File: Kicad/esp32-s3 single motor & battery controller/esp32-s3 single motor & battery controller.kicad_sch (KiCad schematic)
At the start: 61 parts, among them J1 JST SH SM04B/Qwiic, J2 7 pin FPC 0.3mm, J3 Conn_01x03, J4 Conn_01x03, SW1 KMR2, SW2 KMR2, U5 ESP32-S3, U6 74HC595, Y1 40mhz, 10ppm

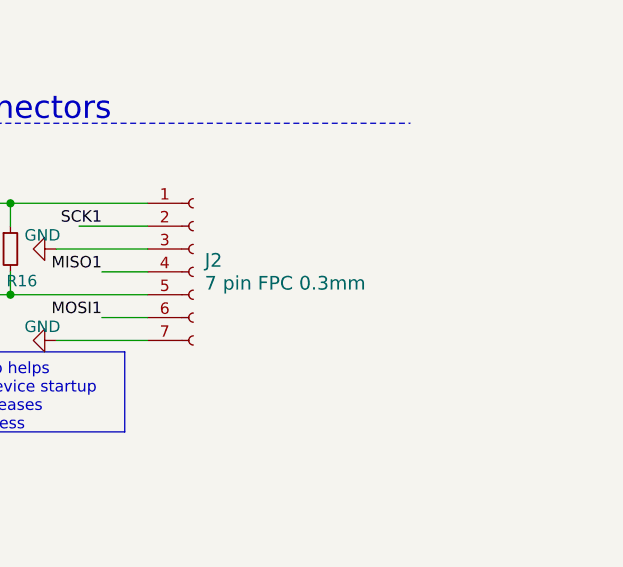
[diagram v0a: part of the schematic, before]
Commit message: Updated README with current progress and V2 pcb
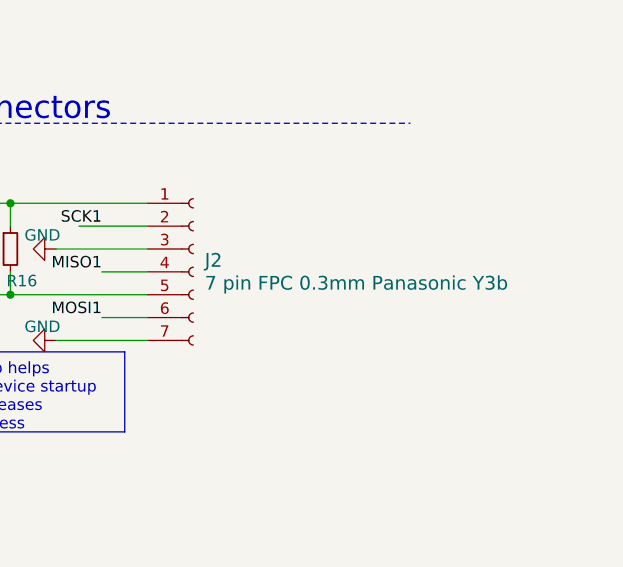
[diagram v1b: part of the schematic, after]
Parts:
- J2: value 7 pin FPC 0.3mm -> 7 pin FPC 0.3mm Panasonic Y3b
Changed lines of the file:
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@@
 			)
 		)
-		(property "Value" "7 pin FPC 0.3mm"
+		(property "Value" "7 pin FPC 0.3mm Panasonic Y3b"
 			(at 261.62 91.4399 0)
 			(effects

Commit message: Gerbers and BOM for v0.4 PCB
I adjusted all the testpoints to be excluded from the BOM.
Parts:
- TP1, TP10, TP11, TP12, TP14, TP15, TP19, TP20, TP21, TP24, TP25, TP26, TP27, TP28, TP29, TP30, TP5, TP7, TP8, TP9: now left out of the parts list
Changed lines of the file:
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@@
 		(unit 1)
 		(exclude_from_sim no)
-		(in_bom yes)
+		(in_bom no)
 		(on_board yes)
 		(dnp no)
@@
 		(unit 1)
 		(exclude_from_sim no)
-		(in_bom yes)
+		(in_bom no)
 		(on_board yes)
 		(dnp no)
@@
 		(unit 1)
 		(exclude_from_sim no)
-		(in_bom yes)
+		(in_bom no)
 		(on_board yes)
 		(dnp no)
@@
 		(unit 1)
 		(exclude_from_sim no)
-		(in_bom yes)
+		(in_bom no)
 		(on_board yes)
 		(dnp no)
@@
 		(unit 1)
 		(exclude_from_sim no)
-		(in_bom yes)
+		(in_bom no)
 		(on_board yes)
 		(dnp no)
@@
 		(unit 1)
 		(exclude_from_sim no)
-		(in_bom yes)
+		(in_bom no)
 		(on_board yes)
 		(dnp no)
@@
 		(unit 1)
 		(exclude_from_sim no)
-		(in_bom yes)
+		(in_bom no)
 		(on_board yes)
 		(dnp no)
@@
 		(unit 1)
 		(exclude_from_sim no)
-		(in_bom yes)
+		(in_bom no)
 		(on_board yes)
 		(dnp no)
@@
 		(unit 1)
 		(exclude_from_sim no)
-		(in_bom yes)
+		(in_bom no)
 		(on_board yes)
 		(dnp no)
@@
 		(unit 1)
 		(exclude_from_sim no)
-		(in_bom yes)
+		(in_bom no)
 		(on_board yes)
 		(dnp no)
@@
 		(unit 1)
 		(exclude_from_sim no)
-		(in_bom yes)
+		(in_bom no)
 		(on_board yes)
 		(dnp no)
@@
 		(unit 1)
 		(exclude_from_sim no)
-		(in_bom yes)
+		(in_bom no)
 		(on_board yes)
 		(dnp no)
@@
 		(unit 1)
 		(exclude_from_sim no)
-		(in_bom yes)
+		(in_bom no)
 		(on_board yes)
 		(dnp no)
@@
 		(unit 1)
 		(exclude_from_sim no)
-		(in_bom yes)
+		(in_bom no)
 		(on_board yes)
 		(dnp no)
@@
 		(unit 1)
 		(exclude_from_sim no)
-		(in_bom yes)
+		(in_bom no)
 		(on_board yes)
 		(dnp no)
@@
 		(unit 1)
 		(exclude_from_sim no)
-		(in_bom yes)
+		(in_bom no)
 		(on_board yes)
 		(dnp no)
@@
 		(unit 1)
 		(exclude_from_sim no)
-		(in_bom yes)
+		(in_bom no)
 		(on_board yes)
 		(dnp no)
@@
 		(unit 1)
 		(exclude_from_sim no)
-		(in_bom yes)
+		(in_bom no)
 		(on_board yes)
 		(dnp no)
@@
 		(unit 1)
 		(exclude_from_sim no)
-		(in_bom yes)
+		(in_bom no)
 		(on_board yes)
 		(dnp no)
@@
 		(unit 1)
 		(exclude_from_sim no)
-		(in_bom yes)
+		(in_bom no)
 		(on_board yes)
 		(dnp no)
